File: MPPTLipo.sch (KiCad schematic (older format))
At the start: 13 parts, among them IC1 SPV1040, P1 CONN_01X01, P2 SmdPad

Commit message: neu
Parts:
- removed P2: SmdPad, franzlibtest:SmdPadFranz, symbol SmdPad
- R4: value R -> 10k
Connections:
- net at C3.2, IC1.4 (VOUT), R1.1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: now also D1.1 (K); no longer D1.2 (A)
- net at IC1.3 (LX), L1.2: now also D1.2 (A); no longer D1.1 (K)
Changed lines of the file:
@@
 P 7350 2650
 F 0 "R4" V 7430 2650 50  0000 C CNN
-F 1 "R" V 7350 2650 50  0000 C CNN
+F 1 "10k" V 7350 2650 50  0000 C CNN
 F 2 "Resistors_SMD:R_0603_HandSoldering" V 7280 2650 50  0001 C CNN
 F 3 "" H 7350 2650 50  0000 C CNN
@@
 F 3 "" H 5050 2050 50  0000 C CNN
 	1    5050 2050
-	1    0    0    -1
+	-1   0    0    1
 $EndComp
 $Comp
@@
 	5700 2600 5700 2050
 Wire Wire Line
-	5700 2050 5200 2050
-Wire Wire Line
-	4900 2050 3850 2050
-Wire Wire Line
 	3850 2050 3850 2550
 Wire Wire Line
@@
 	0    -1   -1   0
 $EndComp
-$Comp
-L SmdPad P2
-U 1 1 58A3448C
-P 3500 3250
-F 0 "P2" H 3500 3250 60  0000 C CNN
-F 1 "SmdPad" H 3600 3300 4   0000 C CNN
-F 2 "franzlibtest:SmdPadFranz" H 3500 3250 60  0001 C CNN
-F 3 "" H 3500 3250 60  0001 C CNN
-	1    3500 3250
-	-1   0    0    1
-$EndComp
-$Comp
-L GND #PWR05
-U 1 1 58A3465C
-P 3500 3350
-F 0 "#PWR05" H 3500 3100 50  0001 C CNN
-F 1 "GND" H 3500 3200 50  0000 C CNN
-F 2 "" H 3500 3350 50  0000 C CNN
-F 3 "" H 3500 3350 50  0000 C CNN
-	1    3500 3350
-	1    0    0    -1
-$EndComp
+Wire Wire Line
+	4900 2050 3850 2050
+Wire Wire Line
+	5700 2050 5200 2050
 $EndSCHEMATC

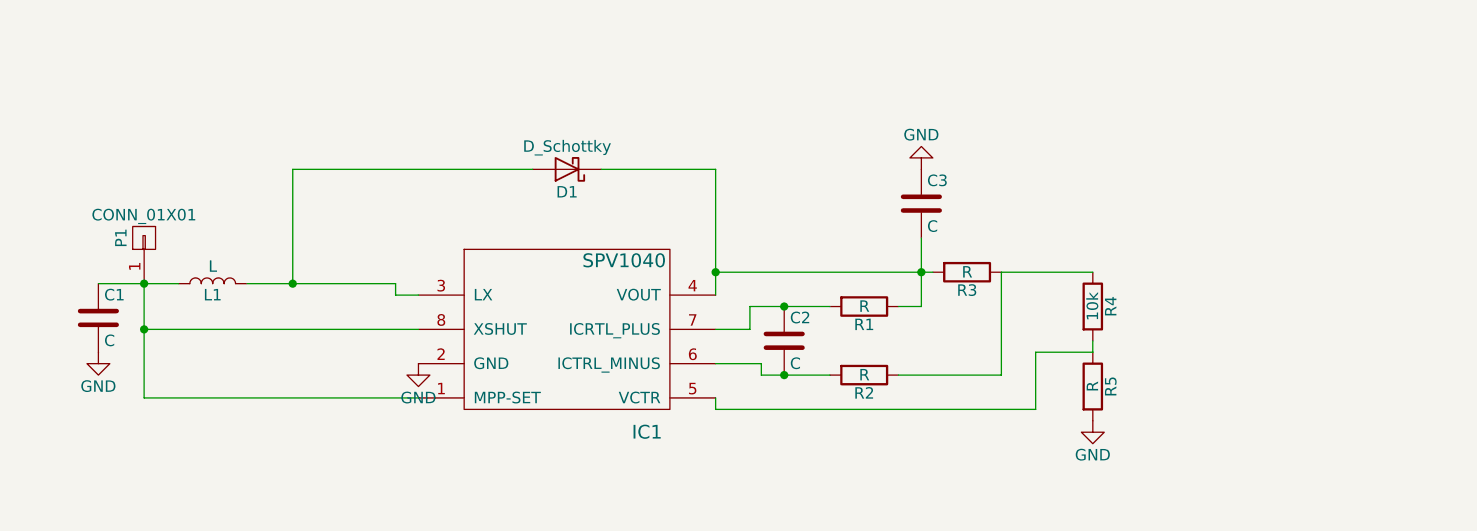
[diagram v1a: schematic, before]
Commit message: Lipoprotektionsmodul
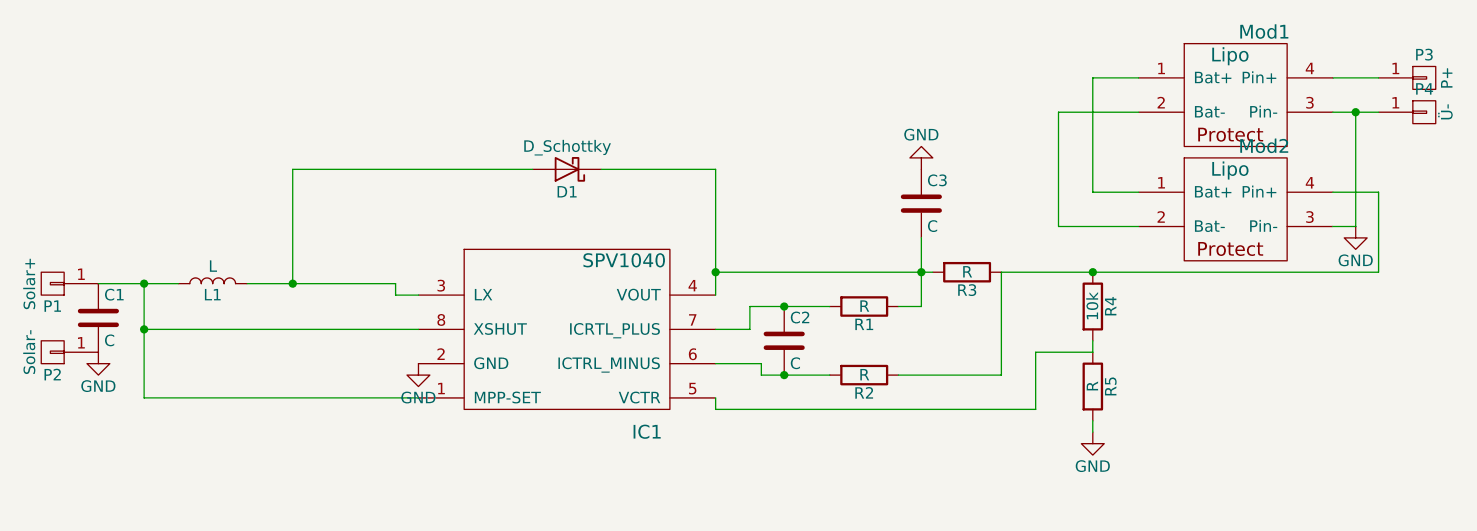
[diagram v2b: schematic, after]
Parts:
- added Mod1, Mod2: Lipo, franzlibtest:LipoProtectPCB, symbol Lipo
- added P2: Solar-, Measurement_Points:Measurement_Point_Square-SMD-Pad_Big, symbol CONN_01X01
- added P3: P+, Measurement_Points:Measurement_Point_Square-SMD-Pad_Big, symbol CONN_01X01
- added P4: Ü-, Measurement_Points:Measurement_Point_Square-SMD-Pad_Big, symbol CONN_01X01
- P1: value CONN_01X01 -> Solar+; footprint Connectors:1pin -> Measurement_Points:Measurement_Point_Square-SMD-Pad_Big
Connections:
- net GND: now also Mod1.3 (Pin-), Mod2.3 (Pin-), P2.1 (P1), P4.1 (P1)
- net at R2.1, R3.1, R4.1: now also Mod2.4 (Pin+)
- new net: Mod1.1 (Bat+), Mod2.1 (Bat+)
- new net: Mod1.2 (Bat-), Mod2.2 (Bat-)
- new net: Mod1.4 (Pin+), P3.1 (P1)
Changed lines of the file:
@@
 	6950 2950 6950 2500
 Wire Wire Line
-	6950 2500 7350 2500
+	6950 2500 8600 2500
 Wire Wire Line
 	7350 2800 7350 2850
@@
 L GND #PWR01
 U 1 1 58A34E75
-P 7350 3150
-F 0 "#PWR01" H 7350 2900 50  0001 C CNN
-F 1 "GND" H 7350 3000 50  0000 C CNN
-F 2 "" H 7350 3150 50  0000 C CNN
-F 3 "" H 7350 3150 50  0000 C CNN
-	1    7350 3150
+P 7350 3200
+F 0 "#PWR01" H 7350 2950 50  0001 C CNN
+F 1 "GND" H 7350 3050 50  0000 C CNN
+F 2 "" H 7350 3200 50  0000 C CNN
+F 3 "" H 7350 3200 50  0000 C CNN
+	1    7350 3200
 	1    0    0    -1
 $EndComp
@@
 	1    0    0    -1
 $EndComp
-$Comp
-L CONN_01X01 P1
-U 1 1 58A35050
-P 3200 2350
-F 0 "P1" H 3200 2450 50  0000 C CNN
-F 1 "CONN_01X01" V 3300 2350 50  0000 C CNN
-F 2 "Connectors:1pin" H 3200 2350 50  0001 C CNN
-F 3 "" H 3200 2350 50  0000 C CNN
-	1    3200 2350
-	0    -1   -1   0
-$EndComp
 Wire Wire Line
 	4900 2050 3850 2050
 Wire Wire Line
 	5700 2050 5200 2050
+$Comp
+L Lipo Mod1
+U 1 1 58A72DFA
+P 7750 2000
+F 0 "Mod1" H 8100 2550 60  0000 C CNN
+F 1 "Lipo" H 7950 2450 60  0000 C CNN
+F 2 "franzlibtest:LipoProtectPCB" H 7750 1650 60  0001 C CNN
+F 3 "" H 7750 1650 60  0001 C CNN
+	1    7750 2000
+	1    0    0    -1
+$EndComp
+$Comp
+L Lipo Mod2
+U 1 1 58A72E7D
+P 7750 2500
+F 0 "Mod2" H 8100 3050 60  0000 C CNN
+F 1 "Lipo" H 7950 2950 60  0000 C CNN
+F 2 "franzlibtest:LipoProtectPCB" H 7750 2150 60  0001 C CNN
+F 3 "" H 7750 2150 60  0001 C CNN
+	1    7750 2500
+	1    0    0    -1
+$EndComp
+Wire Wire Line
+	7550 1650 7350 1650
+Wire Wire Line
+	7350 1650 7350 2150
+Wire Wire Line
+	7350 2150 7550 2150
+Wire Wire Line
+	7550 2300 7200 2300
+Wire Wire Line
+	7200 2300 7200 1800
+Wire Wire Line
+	7200 1800 7550 1800
+Wire Wire Line
+	8400 2300 8500 2300
+Wire Wire Line
+	8500 2300 8500 1800
+Wire Wire Line
+	8400 1800 8600 1800
+Wire Wire Line
+	8400 1650 8600 1650
+Wire Wire Line
+	8600 2150 8400 2150
+$Comp
+L GND #PWR05
+U 1 1 58A730F5
+P 8500 2300
+F 0 "#PWR05" H 8500 2050 50  0001 C CNN
+F 1 "GND" H 8500 2150 50  0000 C CNN
+F 2 "" H 8500 2300 50  0000 C CNN
+F 3 "" H 8500 2300 50  0000 C CNN
+	1    8500 2300
+	1    0    0    -1
+$EndComp
+Wire Wire Line
+	8600 2500 8600 2150
+Connection ~ 7350 2500
+$Comp
+L CONN_01X01 P3
+U 1 1 58A731FD
+P 8800 1650
+F 0 "P3" H 8800 1750 50  0000 C CNN
+F 1 "P+" V 8900 1650 50  0000 C CNN
+F 2 "Measurement_Points:Measurement_Point_Square-SMD-Pad_Big" H 8800 1650 50  0001 C CNN
+F 3 "" H 8800 1650 50  0000 C CNN
+	1    8800 1650
+	1    0    0    -1
+$EndComp
+$Comp
+L CONN_01X01 P4
+U 1 1 58A733DA
+P 8800 1800
+F 0 "P4" H 8800 1900 50  0000 C CNN
+F 1 "Ü-" V 8900 1800 50  0000 C CNN
+F 2 "Measurement_Points:Measurement_Point_Square-SMD-Pad_Big" H 8800 1800 50  0001 C CNN
+F 3 "" H 8800 1800 50  0000 C CNN
+	1    8800 1800
+	1    0    0    -1
+$EndComp
+$Comp
+L CONN_01X01 P1
+U 1 1 58A73459
+P 2800 2550
+F 0 "P1" H 2800 2650 50  0000 C CNN
+F 1 "Solar+" V 2900 2550 50  0000 C CNN
+F 2 "Measurement_Points:Measurement_Point_Square-SMD-Pad_Big" H 2800 2550 50  0001 C CNN
+F 3 "" H 2800 2550 50  0000 C CNN
+	1    2800 2550
+	-1   0    0    1
+$EndComp
+$Comp
+L CONN_01X01 P2
+U 1 1 58A735AB
+P 2800 2850
+F 0 "P2" H 2800 2950 50  0000 C CNN
+F 1 "Solar-" V 2900 2850 50  0000 C CNN
+F 2 "Measurement_Points:Measurement_Point_Square-SMD-Pad_Big" H 2800 2850 50  0001 C CNN
+F 3 "" H 2800 2850 50  0000 C CNN
+	1    2800 2850
+	-1   0    0    1
+$EndComp
+Connection ~ 8500 1800
+Wire Wire Line
+	7350 3150 7350 3200
 $EndSCHEMATC

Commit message: Layout fast fertig
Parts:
- C2, C3: footprint Capacitors_SMD:C_0603_HandSoldering -> Capacitors_SMD:C_0805_HandSoldering
- D1: value D_Schottky -> NSR0530H; footprint Diodes_SMD:D_0805 -> Diodes_SMD:D_SOD-323_HandSoldering
- L1: value L -> 33u; footprint Choke_SMD:Choke_SMD_Wuerth-WE-PD-Typ-LS_Handsoldering -> franzlibtest:VLS6045EX
- R3: value R -> 0.05R; footprint Resistors_SMD:R_0603_HandSoldering -> Resistors_SMD:R_0805_HandSoldering
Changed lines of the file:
@@
 LIBS:valves
 LIBS:spv1040
+LIBS:video
 LIBS:MPPTLipo-cache
-EELAYER 25 0
+EELAYER 26 0
 EELAYER END
 $Descr A4 11693 8268
@@
 P 6800 2500
 F 0 "R3" V 6880 2500 50  0000 C CNN
-F 1 "R" V 6800 2500 50  0000 C CNN
-F 2 "Resistors_SMD:R_0603_HandSoldering" V 6730 2500 50  0001 C CNN
+F 1 "0.05R" V 6800 2500 50  0000 C CNN
+F 2 "Resistors_SMD:R_0805_HandSoldering" V 6730 2500 50  0001 C CNN
 F 3 "" H 6800 2500 50  0000 C CNN
 	1    6800 2500
@@
 F 0 "C2" H 6025 2900 50  0000 L CNN
 F 1 "C" H 6025 2700 50  0000 L CNN
-F 2 "Capacitors_SMD:C_0603_HandSoldering" H 6038 2650 50  0001 C CNN
+F 2 "Capacitors_SMD:C_0805_HandSoldering" H 6038 2650 50  0001 C CNN
 F 3 "" H 6000 2800 50  0000 C CNN
 	1    6000 2800
@@
 F 0 "C3" H 6625 2300 50  0000 L CNN
 F 1 "C" H 6625 2100 50  0000 L CNN
-F 2 "Capacitors_SMD:C_0603_HandSoldering" H 6638 2050 50  0001 C CNN
+F 2 "Capacitors_SMD:C_0805_HandSoldering" H 6638 2050 50  0001 C CNN
 F 3 "" H 6600 2200 50  0000 C CNN
 	1    6600 2200
@@
 P 5050 2050
 F 0 "D1" H 5050 2150 50  0000 C CNN
-F 1 "D_Schottky" H 5050 1950 50  0000 C CNN
-F 2 "Diodes_SMD:D_0805" H 5050 2050 50  0001 C CNN
+F 1 "NSR0530H" H 5050 1950 50  0000 C CNN
+F 2 "Diodes_SMD:D_SOD-323_HandSoldering" H 5050 2050 50  0001 C CNN
 F 3 "" H 5050 2050 50  0000 C CNN
 	1    5050 2050
@@
 P 3500 2550
 F 0 "L1" V 3450 2550 50  0000 C CNN
-F 1 "L" V 3575 2550 50  0000 C CNN
-F 2 "Choke_SMD:Choke_SMD_Wuerth-WE-PD-Typ-LS_Handsoldering" H 3500 2550 50  0001 C CNN
+F 1 "33u" V 3575 2550 50  0000 C CNN
+F 2 "franzlibtest:VLS6045EX" H 3500 2550 50  0001 C CNN
 F 3 "" H 3500 2550 50  0000 C CNN
 	1    3500 2550
